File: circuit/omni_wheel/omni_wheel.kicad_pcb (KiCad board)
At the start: 2 copper layers, 91.8 x 84.9 mm, 60 parts, among them J1 Conn_01x02_Male, J2 USB_C_Receptacle_USB2.0, J3 Conn_01x06_Male, J4 Conn_01x06_Male, J5 Conn_01x06_Male, Q1 SS8050-G, Q2 SS8050-G, SW1 SW_Push, SW2 SW_Push, SW3 SW_Push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

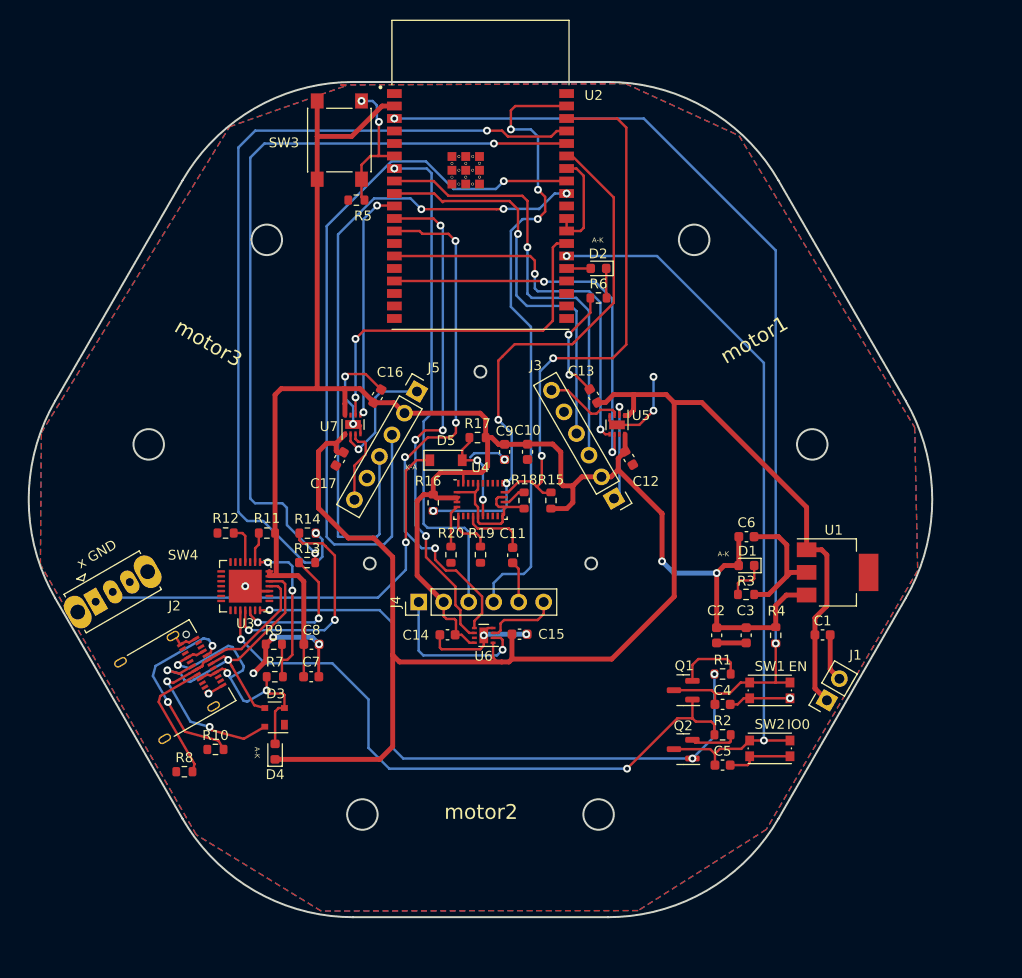
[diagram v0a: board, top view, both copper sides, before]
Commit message: redesign the PCB: the direction of parts.
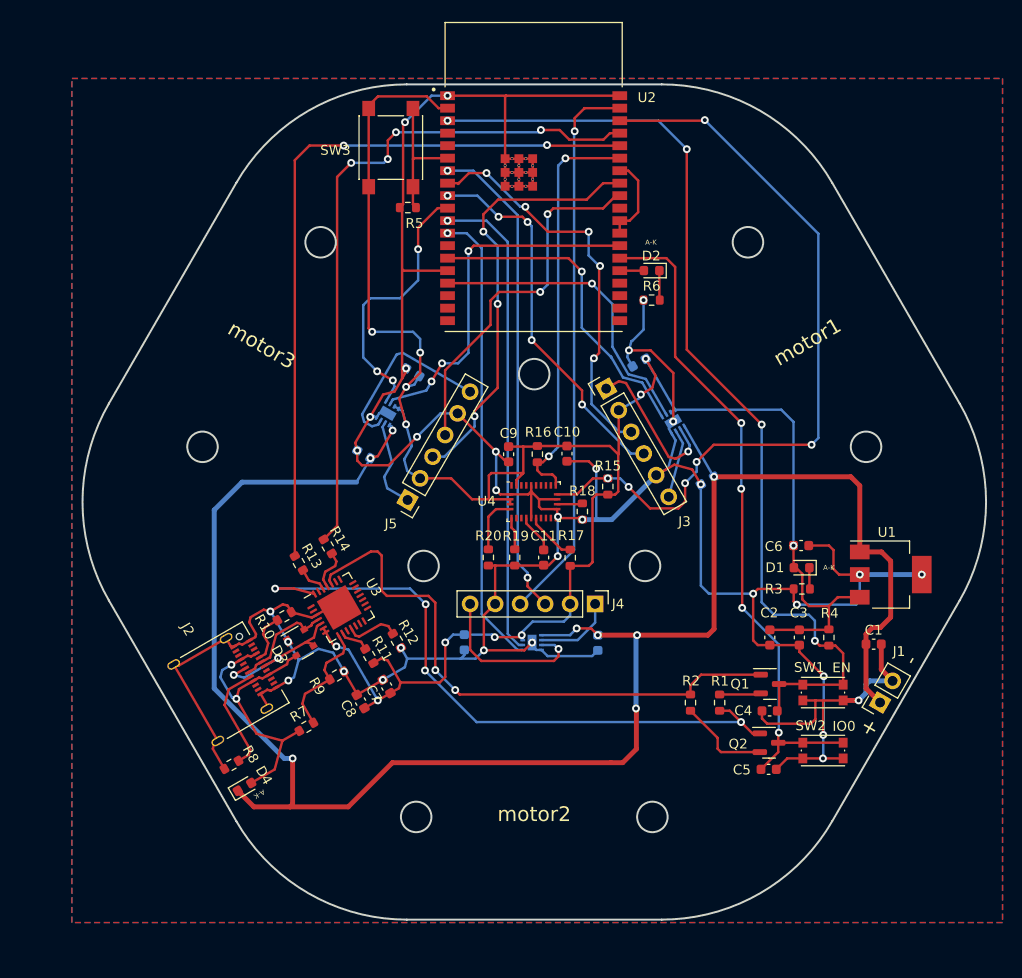
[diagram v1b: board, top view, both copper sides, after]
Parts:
- removed D5: 1N4148W, Diode_SMD:D_SOD-123
- removed SW4: SW_SPDT, Button_Switch_THT:SW_Slide_1P2T_CK_OS102011MS2Q
- C12, C13, C14, C15, C16, C17, U5, U6, U7: moved to B.Cu
- moved R12 20.6 mm to (92.0, 114.2), turned to -60 degrees
- moved J4 17.9 mm to (112.1, 110.4), turned to -90 degrees
- moved R11 16.3 mm to (89.2, 115.7), turned to 120 degrees
- moved R17 15.4 mm to (109.6, 105.7), turned to -90 degrees
- moved R10 15.2 mm to (80.5, 111.7), turned to -150 degrees
- moved C13 14.4 mm to (123.5, 97.9), turned to -150 degrees
- moved R16 11.7 mm to (106.2, 95.2)
- moved J3 11.2 mm to (113.2, 88.6), turned to 30 degrees
- moved J5 11.1 mm to (93.0, 99.9), turned to 150 degrees
- moved U3 9.79 mm to (86.1, 110.8), turned to 30 degrees
- moved C12 9.76 mm to (116.6, 85.9), turned to -150 degrees
- moved Q1 8.83 mm to (129.9, 118.6), turned to 0 degrees
- moved Q2 8.74 mm to (129.8, 124.5), turned to 0 degrees
- moved D3 8.03 mm to (82.1, 114.4), turned to 30 degrees
- moved C15 8.00 mm to (112.4, 114.4), turned to -90 degrees
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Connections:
- U5 pad 7: unconnected-(U5-Pad7) -> +3V3
- U6 pad 7: unconnected-(U6-Pad7) -> +3V3
- U7 pad 7: unconnected-(U7-Pad7) -> +3V3
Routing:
- net GND: track 127.6 -> 387.8 mm, vias 15 -> 32
- net Net-(D5-Pad1): track 44.1 -> 0.00 mm, vias 1 -> 0
- net V_MOT: track 160.0 -> 194.3 mm, vias 0 -> 8
- net motor3_enc_a: track 77.8 -> 43.8 mm, vias 1 -> 3
- net motor3_enc_b: track 68.8 -> 37.3 mm, vias 3 -> 2
- net SCL: track 56.1 -> 78.9 mm, vias 2 -> 6
- net USB_DP: track 31.5 -> 10.2 mm, vias 2 -> 0
- net Net-(R14-Pad1): track 23.0 -> 4.24 mm, vias 2 -> 0
- net +3V3: track 199.4 -> 216.3 mm, vias 2 -> 12
- net USB_DN: track 31.1 -> 14.9 mm
- net TXD0: track 85.2 -> 69.9 mm, vias 2 -> 4
- net Net-(J2-PadA5): track 20.4 -> 5.10 mm, vias 2 -> 0
- net SDA: track 55.0 -> 41.7 mm, vias 3 -> 2
- net Net-(R13-Pad1): track 14.4 -> 3.02 mm, vias 2 -> 0
- net motor3_out2: track 7.97 -> 18.5 mm
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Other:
- outline, holes or cut-outs redrawn
- board text removed: "K-A"
- board text removed: "x GND"

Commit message: Revised based on review 2024 Dec 7th.
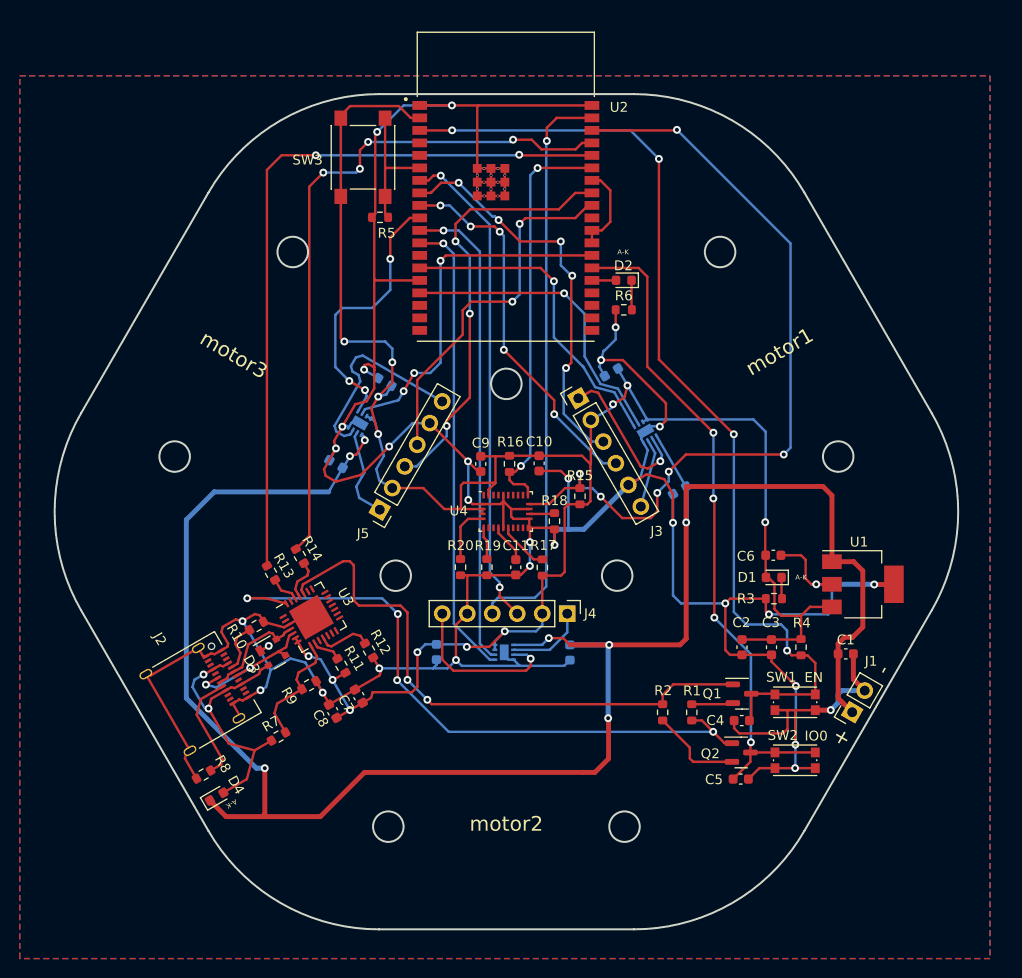
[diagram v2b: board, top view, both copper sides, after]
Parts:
- moved C4 3.00 mm to (127.0, 122.3)
- moved U6 3.00 mm to (102.9, 115.3)
- moved R15 3.00 mm to (110.6, 99.5)
- moved U3 3.00 mm to (83.3, 111.8)
- moved R18 3.00 mm to (108.0, 102.0)
- moved C8 3.00 mm to (85.4, 121.3)
- moved R9 3.00 mm to (83.0, 118.7)
- moved C9 3.00 mm to (100.5, 96.2)
- moved J3 3.00 mm to (110.4, 89.5)
- moved C3 3.00 mm to (130.0, 114.8)
- moved R13 3.00 mm to (79.2, 107.3)
- moved U5 3.00 mm to (117.2, 92.9)
- moved SW2 3.00 mm to (132.4, 126.3)
- moved C15 3.00 mm to (109.5, 115.4)
- moved C13 3.00 mm to (120.7, 98.9)
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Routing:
- net GND: track 387.8 -> 410.9 mm, vias 32 -> 30
- net V_MOT: track 194.3 -> 202.0 mm, vias 8 -> 7
- net SCL: track 78.9 -> 81.8 mm
- net +3V3: track 216.3 -> 213.3 mm, vias 12 -> 13
- net motor3_out2: track 18.5 -> 20.9 mm
- net motor2_enc_b: track 56.7 -> 58.9 mm
